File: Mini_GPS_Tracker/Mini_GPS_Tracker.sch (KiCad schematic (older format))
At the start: 19 parts, among them J1 USB_C_Receptacle, SW1 SW_Push, U1 CH340E, Y1 Crystal

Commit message: updates to routing
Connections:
- wire segments 79 -> 81
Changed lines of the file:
@@
 Wire Wire Line
 	5950 950  5950 1050
-Text GLabel 10550 4350 2    50   Input ~ 0
-GPS_TX
-Text GLabel 10550 4450 2    50   Input ~ 0
-GPS_RX
-Wire Wire Line
-	10300 4350 10550 4350
-Wire Wire Line
-	10300 4450 10550 4450
 Text GLabel 10500 5050 2    50   Input ~ 0
 TRANS_TX
@@
 Text GLabel 7650 3250 2    50   Input ~ 0
 TRANS_RX
+Wire Wire Line
+	10300 4350 10550 4350
+Wire Wire Line
+	10300 4450 10550 4450
+Text GLabel 10550 4450 2    50   Input ~ 0
+GPS_RX
+Text GLabel 10550 4350 2    50   Input ~ 0
+GPS_TX
+Text GLabel 7800 4750 2    50   Input ~ 0
+GPS_RX
+Text GLabel 7800 4650 2    50   Input ~ 0
+GPS_TX
+Wire Wire Line
+	7650 4650 7800 4650
+Wire Wire Line
+	7650 4750 7800 4750
 $EndSCHEMATC

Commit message: worked on routing
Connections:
- wire segments 81 -> 83
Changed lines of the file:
@@
 Comment4 ""
 $EndDescr
-$Sheet
-S 8950 4950 1350 500
-U 5E70A48E
-F0 "Transmitter" 50
-F1 "Transmitter.sch" 50
-F2 "TX" I R 10300 5050 50
-F3 "RX" I R 10300 5150 50
-$EndSheet
-$Sheet
-S 8950 4250 1350 500
-U 5E70A878
-F0 "GPS" 50
-F1 "GPS.sch" 50
-F2 "TX" I R 10300 4350 50
-F3 "RX" I R 10300 4450 50
-$EndSheet
-$Sheet
-S 8950 3450 1350 450
-U 5E70B79C
-F0 "Sheet5E70B79B" 50
-F1 "Power.sch" 50
-$EndSheet
 $Comp
 L Device:Crystal Y1
@@
 Wire Wire Line
 	5950 950  5950 1050
-Text GLabel 10500 5050 2    50   Input ~ 0
-TRANS_TX
-Text GLabel 10500 5150 2    50   Input ~ 0
-TRANS_RX
-Wire Wire Line
-	10300 5050 10500 5050
-Wire Wire Line
-	10300 5150 10500 5150
-Text GLabel 10400 2700 2    50   Input ~ 0
-Pressure_SCL
-Text GLabel 10400 2800 2    50   Input ~ 0
-Pressure_SDA
-Wire Wire Line
-	10350 2700 10400 2700
-Wire Wire Line
-	10350 2800 10400 2800
 $Comp
 L Sparkfun~Artemis:CH340E U1
@@
 Wire Wire Line
 	4450 4450 4450 4350
-$Sheet
-S 8900 2550 1450 550
-U 5E70BD5E
-F0 "Sheet5E70BD5D" 50
-F1 "Sensor.sch" 50
-F2 "SCL" I R 10350 2700 50
-F3 "SDA" I R 10350 2800 50
-$EndSheet
 $Comp
 L Sparkfun~Artemis:SPARKFUN_WRL-15376 MD1
@@
 Text GLabel 7650 3250 2    50   Input ~ 0
 TRANS_RX
-Wire Wire Line
-	10300 4350 10550 4350
-Wire Wire Line
-	10300 4450 10550 4450
-Text GLabel 10550 4450 2    50   Input ~ 0
-GPS_RX
-Text GLabel 10550 4350 2    50   Input ~ 0
-GPS_TX
 Text GLabel 7800 4750 2    50   Input ~ 0
 GPS_RX
@@
 Wire Wire Line
 	7650 4750 7800 4750
+Text GLabel 7850 1550 2    50   Input ~ 0
+Pressure_SDA
+Text GLabel 7850 1450 2    50   Input ~ 0
+Pressure_SCL
+Wire Wire Line
+	7650 1450 7850 1450
+Wire Wire Line
+	7650 1550 7850 1550
+Text GLabel 10650 4250 2    50   Input ~ 0
+GPS_TX
+Text GLabel 10650 4350 2    50   Input ~ 0
+GPS_RX
+Wire Wire Line
+	10400 4350 10650 4350
+Wire Wire Line
+	10400 4250 10650 4250
+$Sheet
+S 9000 2450 1450 550
+U 5E70BD5E
+F0 "Sheet5E70BD5D" 50
+F1 "Sensor.sch" 50
+F2 "SCL" I R 10450 2600 50
+F3 "SDA" I R 10450 2700 50
+$EndSheet
+Wire Wire Line
+	10450 2700 10500 2700
+Wire Wire Line
+	10450 2600 10500 2600
+Text GLabel 10500 2700 2    50   Input ~ 0
+Pressure_SDA
+Text GLabel 10500 2600 2    50   Input ~ 0
+Pressure_SCL
+Wire Wire Line
+	10400 5050 10600 5050
+Wire Wire Line
+	10400 4950 10600 4950
+Text GLabel 10600 5050 2    50   Input ~ 0
+TRANS_RX
+Text GLabel 10600 4950 2    50   Input ~ 0
+TRANS_TX
+$Sheet
+S 9050 3350 1350 450
+U 5E70B79C
+F0 "Sheet5E70B79B" 50
+F1 "Power.sch" 50
+$EndSheet
+$Sheet
+S 9050 4150 1350 500
+U 5E70A878
+F0 "GPS" 50
+F1 "GPS.sch" 50
+F2 "TX" I R 10400 4250 50
+F3 "RX" I R 10400 4350 50
+$EndSheet
+$Sheet
+S 9050 4850 1350 500
+U 5E70A48E
+F0 "Transmitter" 50
+F1 "Transmitter.sch" 50
+F2 "TX" I R 10400 4950 50
+F3 "RX" I R 10400 5050 50
+$EndSheet
 $EndSCHEMATC

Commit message: updated antenna;
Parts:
- SW1: footprint Button_Switch_SMD:SW_DIP_SPSTx01_Slide_6.7x4.1mm_W6.73mm_P2.54mm_LowProfile_JPin -> Button_Switch_SMD:SW_MEC_5GSH9
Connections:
- net labels removed: RX0
- wire segments 83 -> 85
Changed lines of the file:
@@
 $EndComp
 $Comp
-L power:GND #PWR0101
+L power:GND #PWR011
 U 1 1 5E71F955
 P 4100 2100
-F 0 "#PWR0101" H 4100 1850 50  0001 C CNN
+F 0 "#PWR011" H 4100 1850 50  0001 C CNN
 F 1 "GND" H 4105 1927 50  0000 C CNN
 F 2 "" H 4100 2100 50  0001 C CNN
@@
 $EndComp
 $Comp
-L power:GND #PWR0102
+L power:GND #PWR01
 U 1 1 5E72C86A
 P 1100 1400
-F 0 "#PWR0102" H 1100 1150 50  0001 C CNN
+F 0 "#PWR01" H 1100 1150 50  0001 C CNN
 F 1 "GND" H 1105 1227 50  0000 C CNN
 F 2 "" H 1100 1400 50  0001 C CNN
@@
 $EndComp
 $Comp
-L power:GND #PWR0103
+L power:GND #PWR05
 U 1 1 5E72D50D
 P 1800 1400
-F 0 "#PWR0103" H 1800 1150 50  0001 C CNN
+F 0 "#PWR05" H 1800 1150 50  0001 C CNN
 F 1 "GND" H 1805 1227 50  0000 C CNN
 F 2 "" H 1800 1400 50  0001 C CNN
@@
 F 0 "SW1" V 1646 2852 50  0000 R CNN
 F 1 "SW_Push" V 1555 2852 50  0000 R CNN
-F 2 "Button_Switch_SMD:SW_DIP_SPSTx01_Slide_6.7x4.1mm_W6.73mm_P2.54mm_LowProfile_JPin" H 1600 3100 50  0001 C CNN
+F 2 "Button_Switch_SMD:SW_MEC_5GSH9" H 1600 3100 50  0001 C CNN
 F 3 "~" H 1600 3100 50  0001 C CNN
 	1    1600 2900
@@
 $EndComp
 $Comp
-L power:GND #PWR0104
+L power:GND #PWR04
 U 1 1 5E737F92
 P 1600 3400
-F 0 "#PWR0104" H 1600 3150 50  0001 C CNN
+F 0 "#PWR04" H 1600 3150 50  0001 C CNN
 F 1 "GND" H 1605 3227 50  0000 C CNN
 F 2 "" H 1600 3400 50  0001 C CNN
@@
 $EndComp
 $Comp
-L power:GND #PWR0105
+L power:GND #PWR08
 U 1 1 5E738744
 P 2200 3400
-F 0 "#PWR0105" H 2200 3150 50  0001 C CNN
+F 0 "#PWR08" H 2200 3150 50  0001 C CNN
 F 1 "GND" H 2205 3227 50  0000 C CNN
 F 2 "" H 2200 3400 50  0001 C CNN
@@
 	5950 1450 6150 1450
 $Comp
-L power:+3.3V #PWR0106
+L power:+3.3V #PWR014
 U 1 1 5E73F797
 P 5950 750
-F 0 "#PWR0106" H 5950 600 50  0001 C CNN
+F 0 "#PWR014" H 5950 600 50  0001 C CNN
 F 1 "+3.3V" H 5965 923 50  0000 C CNN
 F 2 "" H 5950 750 50  0001 C CNN
@@
 $EndComp
 $Comp
-L power:GND #PWR0107
+L power:GND #PWR010
 U 1 1 5E74D69E
 P 3050 5600
-F 0 "#PWR0107" H 3050 5350 50  0001 C CNN
+F 0 "#PWR010" H 3050 5350 50  0001 C CNN
 F 1 "GND" H 3055 5427 50  0000 C CNN
 F 2 "" H 3050 5600 50  0001 C CNN
@@
 	3050 5450 3050 5600
 $Comp
-L power:+3.3V #PWR0108
+L power:+3.3V #PWR06
 U 1 1 5E74F6B2
 P 1950 4850
-F 0 "#PWR0108" H 1950 4700 50  0001 C CNN
+F 0 "#PWR06" H 1950 4700 50  0001 C CNN
 F 1 "+3.3V" H 1965 5023 50  0000 C CNN
 F 2 "" H 1950 4850 50  0001 C CNN
@@
 $EndComp
 $Comp
-L power:GND #PWR0109
+L power:GND #PWR09
 U 1 1 5E75A19B
 P 2650 6050
-F 0 "#PWR0109" H 2650 5800 50  0001 C CNN
+F 0 "#PWR09" H 2650 5800 50  0001 C CNN
 F 1 "GND" H 2655 5877 50  0000 C CNN
 F 2 "" H 2650 6050 50  0001 C CNN
@@
 	2650 6050 2650 5900
 $Comp
-L power:GND #PWR0110
+L power:GND #PWR02
 U 1 1 5E7614F5
 P 1200 7350
-F 0 "#PWR0110" H 1200 7100 50  0001 C CNN
+F 0 "#PWR02" H 1200 7100 50  0001 C CNN
 F 1 "GND" H 1205 7177 50  0000 C CNN
 F 2 "" H 1200 7350 50  0001 C CNN
@@
 $EndComp
 $Comp
-L power:GND #PWR0111
+L power:GND #PWR07
 U 1 1 5E77454B
 P 2150 6050
-F 0 "#PWR0111" H 2150 5800 50  0001 C CNN
+F 0 "#PWR07" H 2150 5800 50  0001 C CNN
 F 1 "GND" H 2155 5877 50  0000 C CNN
 F 2 "" H 2150 6050 50  0001 C CNN
@@
 	3950 5150 4150 5150
 $Comp
-L power:+3.3V #PWR0112
+L power:+3.3V #PWR012
 U 1 1 5E7841FA
 P 4200 3950
-F 0 "#PWR0112" H 4200 3800 50  0001 C CNN
+F 0 "#PWR012" H 4200 3800 50  0001 C CNN
 F 1 "+3.3V" H 4215 4123 50  0000 C CNN
 F 2 "" H 4200 3950 50  0001 C CNN
@@
 $EndComp
 $Comp
-L power:+3.3V #PWR0113
+L power:+3.3V #PWR013
 U 1 1 5E78507D
 P 4450 3950
-F 0 "#PWR0113" H 4450 3800 50  0001 C CNN
+F 0 "#PWR013" H 4450 3800 50  0001 C CNN
 F 1 "+3.3V" H 4465 4123 50  0000 C CNN
 F 2 "" H 4450 3950 50  0001 C CNN
@@
 $EndComp
 $Comp
-L power:GND #PWR0114
+L power:GND #PWR015
 U 1 1 5E7E1693
 P 7750 6400
-F 0 "#PWR0114" H 7750 6150 50  0001 C CNN
+F 0 "#PWR015" H 7750 6150 50  0001 C CNN
 F 1 "GND" H 7755 6227 50  0000 C CNN
 F 2 "" H 7750 6400 50  0001 C CNN
@@
 Wire Wire Line
 	7750 6350 7750 6400
+Text GLabel 7800 1050 2    50   Input ~ 0
+TXO
 Text GLabel 7800 1150 2    50   Input ~ 0
-TXO
-Text GLabel 7800 1050 2    50   Input ~ 0
-RX0
+RXI
+Wire Wire Line
+	7650 1150 7800 1150
 Wire Wire Line
 	7650 1050 7800 1050
-Wire Wire Line
-	7650 1150 7800 1150
-$Comp
-L power:+3.3V #PWR0115
+$Comp
+L power:+3.3V #PWR03
 U 1 1 5E7FD57A
 P 1600 1950
-F 0 "#PWR0115" H 1600 1800 50  0001 C CNN
+F 0 "#PWR03" H 1600 1800 50  0001 C CNN
 F 1 "+3.3V" H 1615 2123 50  0000 C CNN
 F 2 "" H 1600 1950 50  0001 C CNN
@@
 	1    0    0    -1
 $EndComp
-Text GLabel 7650 3150 2    50   Input ~ 0
+Text GLabel 7850 3250 2    50   Input ~ 0
 TRANS_TX
-Text GLabel 7650 3250 2    50   Input ~ 0
+Text GLabel 7850 3150 2    50   Input ~ 0
 TRANS_RX
-Text GLabel 7800 4750 2    50   Input ~ 0
+Text GLabel 7800 4650 2    50   Input ~ 0
 GPS_RX
-Text GLabel 7800 4650 2    50   Input ~ 0
-GPS_TX
-Wire Wire Line
-	7650 4650 7800 4650
 Wire Wire Line
 	7650 4750 7800 4750
@@
 F3 "RX" I R 10400 5050 50
 $EndSheet
+Wire Wire Line
+	7650 3150 7850 3150
+Wire Wire Line
+	7650 3250 7850 3250
+Wire Wire Line
+	7650 4650 7800 4650
+Text GLabel 7800 4750 2    50   Input ~ 0
+GPS_TX
 $EndSCHEMATC

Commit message: added 9dof
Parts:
- added J4: Conn_ARM_JTAG_SWD_10, Connector_PinHeader_1.00mm:PinHeader_2x05_P1.00mm_Vertical, symbol Connector:Conn_ARM_JTAG_SWD_10
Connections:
- net labels added: A1, RESET_2, SWDCK, SWDIO
- net labels removed: DTR
- wire segments 85 -> 100
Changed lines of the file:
@@
 	5900 1250 6150 1250
 Text GLabel 1000 1000 0    50   Input ~ 0
-DTR
+RTS
 Text GLabel 1900 1000 2    50   Input ~ 0
 BOOT
@@
 Connection ~ 1800 1000
 Text GLabel 850  2700 0    50   Input ~ 0
-DTR
+RTS
 Text GLabel 2300 2700 2    50   Input ~ 0
 RESET
@@
 Text GLabel 7800 4750 2    50   Input ~ 0
 GPS_TX
+$Comp
+L Connector:Conn_ARM_JTAG_SWD_10 J4
+U 1 1 5E76D592
+P 4950 6900
+F 0 "J4" H 4507 6946 50  0000 R CNN
+F 1 "Conn_ARM_JTAG_SWD_10" H 4507 6855 50  0000 R CNN
+F 2 "Connector_PinHeader_1.00mm:PinHeader_2x05_P1.00mm_Vertical" H 4950 6900 50  0001 C CNN
+F 3 "http://infocenter.arm.com/help/topic/com.arm.doc.ddi0314h/DDI0314H_coresight_components_trm.pdf" V 4600 5650 50  0001 C CNN
+	1    4950 6900
+	1    0    0    -1
+$EndComp
+$Comp
+L power:+3.3V #PWR030
+U 1 1 5E76F259
+P 4950 6150
+F 0 "#PWR030" H 4950 6000 50  0001 C CNN
+F 1 "+3.3V" H 4965 6323 50  0000 C CNN
+F 2 "" H 4950 6150 50  0001 C CNN
+F 3 "" H 4950 6150 50  0001 C CNN
+	1    4950 6150
+	1    0    0    -1
+$EndComp
+$Comp
+L power:GND #PWR031
+U 1 1 5E76F975
+P 4950 7600
+F 0 "#PWR031" H 4950 7350 50  0001 C CNN
+F 1 "GND" H 4955 7427 50  0000 C CNN
+F 2 "" H 4950 7600 50  0001 C CNN
+F 3 "" H 4950 7600 50  0001 C CNN
+	1    4950 7600
+	1    0    0    -1
+$EndComp
+Wire Wire Line
+	4950 7500 4950 7550
+Wire Wire Line
+	4850 7500 4850 7550
+Wire Wire Line
+	4850 7550 4950 7550
+Connection ~ 4950 7550
+Wire Wire Line
+	4950 7550 4950 7600
+Wire Wire Line
+	4950 6300 4950 6150
+Text GLabel 5600 7000 2    50   Input ~ 0
+A1
+Text GLabel 5550 6600 2    50   Input ~ 0
+RESET_2
+Text GLabel 5600 6900 2    50   Input ~ 0
+SWDIO
+Text GLabel 5600 6800 2    50   Input ~ 0
+SWDCK
+Wire Wire Line
+	5450 6600 5550 6600
+Wire Wire Line
+	5450 6800 5600 6800
+Wire Wire Line
+	5450 6900 5600 6900
+Wire Wire Line
+	5450 7000 5600 7000
+Wire Wire Line
+	4950 7550 5550 7550
+Wire Wire Line
+	5550 7550 5550 7100
+Wire Wire Line
+	5550 7100 5450 7100
+Text GLabel 7850 2950 2    50   Input ~ 0
+SWDIO
+Text GLabel 7850 3050 2    50   Input ~ 0
+SWDCK
+Wire Wire Line
+	7650 2950 7850 2950
+Wire Wire Line
+	7650 3050 7850 3050
+Text GLabel 7800 3850 2    50   Input ~ 0
+A1
+Wire Wire Line
+	7650 3850 7800 3850
 $EndSCHEMATC

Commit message: schamatics finalized
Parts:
- removed C2: CAP, Capacitor_SMD:C_0805_2012Metric_Pad1.15x1.40mm_HandSolder, symbol pspice:CAP
- removed R1: DNP, symbol Device:R
- removed R3: 220K, Resistor_SMD:R_0805_2012Metric_Pad1.15x1.40mm_HandSolder, symbol Device:R
- added H1, H2, H3, H4: MountingHole_Pad, MountingHole:MountingHole_3.2mm_M3, symbol Mechanical:MountingHole_Pad
- SW1: footprint Button_Switch_SMD:SW_MEC_5GSH9 -> Sparkfun-Artemis:SW_TL1015AF160QG
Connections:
- net labels added: 9_SCL, 9_SDA, MISO_Flash, MOSI_Flash, clk_flash, cs_flash, gps_reset, v_measure
- net labels removed: BOOT, RESET_2, TXO, nReset
- wire segments 100 -> 113
- no-connect marks 0 -> 47
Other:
- moved on the sheet: J4

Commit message: added routing
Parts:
- added LS1: CSS-J4D20-SMT, Sparkfun-Artemis:CUI_CSS-J4D20-SMT, symbol Sparkfun~Artemis:CSS-J4D20-SMT
- added R7: R, Resistor_SMD:R_0805_2012Metric_Pad1.15x1.40mm_HandSolder, symbol Device:R
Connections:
- net labels added: buzzer
- wire segments 113 -> 117
- no-connect marks 47 -> 46
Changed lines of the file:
@@
 NoConn ~ 7650 3550
 NoConn ~ 7650 3450
-NoConn ~ 7650 3350
 NoConn ~ 7650 2850
 NoConn ~ 7650 2750
@@
 Wire Wire Line
 	7650 1750 7850 1750
+$Comp
+L Sparkfun~Artemis:CSS-J4D20-SMT LS1
+U 1 1 5E7E01A2
+P 5300 3750
+F 0 "LS1" H 5405 3796 50  0000 L CNN
+F 1 "CSS-J4D20-SMT" H 5405 3705 50  0000 L CNN
+F 2 "Sparkfun-Artemis:CUI_CSS-J4D20-SMT" H 5300 3750 50  0001 L BNN
+F 3 "CUI" H 5300 3750 50  0001 L BNN
+F 4 "None" H 5300 3750 50  0001 L BNN "Field4"
+F 5 "CSS-J4D20-SMT" H 5300 3750 50  0001 L BNN "Field5"
+F 6 "Unavailable" H 5300 3750 50  0001 L BNN "Field6"
+F 7 "8.5 mm, 3.6 V, 90 dB, Surface Mount _SMT_, Magnetic Audio Transducer Buzzer" H 5300 3750 50  0001 L BNN "Field7"
+F 8 "None" H 5300 3750 50  0001 L BNN "Field8"
+	1    5300 3750
+	1    0    0    -1
+$EndComp
+$Comp
+L Device:R R7
+U 1 1 5E7E2738
+P 5300 3300
+F 0 "R7" H 5370 3346 50  0000 L CNN
+F 1 "R" H 5370 3255 50  0000 L CNN
+F 2 "Resistor_SMD:R_0805_2012Metric_Pad1.15x1.40mm_HandSolder" V 5230 3300 50  0001 C CNN
+F 3 "~" H 5300 3300 50  0001 C CNN
+	1    5300 3300
+	1    0    0    -1
+$EndComp
+$Comp
+L power:GND #PWR0116
+U 1 1 5E7E36E3
+P 5300 4050
+F 0 "#PWR0116" H 5300 3800 50  0001 C CNN
+F 1 "GND" H 5305 3877 50  0000 C CNN
+F 2 "" H 5300 4050 50  0001 C CNN
+F 3 "" H 5300 4050 50  0001 C CNN
+	1    5300 4050
+	1    0    0    -1
+$EndComp
+Wire Wire Line
+	5300 3950 5300 4050
+Wire Wire Line
+	5300 3550 5300 3450
+Text GLabel 5300 3000 1    50   Input ~ 0
+buzzer
+Wire Wire Line
+	5300 3000 5300 3150
+Text GLabel 7850 3350 2    50   Input ~ 0
+buzzer
+Wire Wire Line
+	7650 3350 7850 3350
 $EndSCHEMATC

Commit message: all  artemis connections routed
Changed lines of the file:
@@
 Wire Wire Line
 	7750 6350 7750 6400
-Text GLabel 7800 1050 2    50   Input ~ 0
-TX0
-Text GLabel 7800 1150 2    50   Input ~ 0
-RXI
-Wire Wire Line
-	7650 1150 7800 1150
-Wire Wire Line
-	7650 1050 7800 1050
 $Comp
 L power:+3.3V #PWR03
@@
 	1    0    0    -1
 $EndComp
-Text GLabel 7850 3250 2    50   Input ~ 0
-TRANS_TX
+Text GLabel 7800 3550 2    50   Input ~ 0
+TRANS_RX
 Text GLabel 7850 3150 2    50   Input ~ 0
-TRANS_RX
-Text GLabel 7800 4650 2    50   Input ~ 0
 GPS_RX
-Wire Wire Line
-	7650 4750 7800 4750
-Text GLabel 7850 1550 2    50   Input ~ 0
+Text GLabel 7800 3450 2    50   Input ~ 0
 Pressure_SDA
-Text GLabel 7850 1450 2    50   Input ~ 0
-Pressure_SCL
 Wire Wire Line
 	7650 1450 7850 1450
@@
 Wire Wire Line
 	7650 4650 7800 4650
-Text GLabel 7800 4750 2    50   Input ~ 0
+Text GLabel 7850 3250 2    50   Input ~ 0
 GPS_TX
 $Comp
@@
 Wire Wire Line
 	7650 2550 7800 2550
-Text GLabel 7800 5050 2    50   Input ~ 0
+Text GLabel 7850 1450 2    50   Input ~ 0
 9_SCL
-Text GLabel 7800 5150 2    50   Input ~ 0
+Text GLabel 7850 1550 2    50   Input ~ 0
 9_SDA
-Wire Wire Line
-	7650 5050 7800 5050
-Wire Wire Line
-	7650 5150 7800 5150
-Text GLabel 7800 5250 2    50   Input ~ 0
+Text GLabel 7800 2450 2    50   Input ~ 0
 gps_reset
-Wire Wire Line
-	7650 5250 7800 5250
-NoConn ~ 7650 5550
 NoConn ~ 7650 5450
 NoConn ~ 7650 4950
 NoConn ~ 7650 4850
 NoConn ~ 7650 4550
-NoConn ~ 7650 4450
 NoConn ~ 7650 4350
 NoConn ~ 7650 4250
@@
 NoConn ~ 7650 3950
 NoConn ~ 7650 3750
-NoConn ~ 7650 3650
-NoConn ~ 7650 3550
-NoConn ~ 7650 3450
 NoConn ~ 7650 2850
 NoConn ~ 7650 2750
 NoConn ~ 7650 2650
-NoConn ~ 7650 2450
 NoConn ~ 7650 2350
-NoConn ~ 7650 2250
 NoConn ~ 7650 2150
 NoConn ~ 7650 2050
 NoConn ~ 7650 1350
 NoConn ~ 7650 1250
-NoConn ~ 7650 950
 Text GLabel 5900 1250 0    50   Input ~ 0
 RESET
@@
 Wire Wire Line
 	10450 5900 10600 5900
-Text GLabel 7800 1950 2    50   Input ~ 0
+Text GLabel 7800 4650 2    50   Input ~ 0
 MOSI_Flash
-Text GLabel 7800 1850 2    50   Input ~ 0
+Text GLabel 7800 5150 2    50   Input ~ 0
 MISO_Flash
-Wire Wire Line
-	7650 1850 7800 1850
-Wire Wire Line
-	7650 1950 7800 1950
-Text GLabel 7850 1750 2    50   Input ~ 0
+Text GLabel 7800 950  2    50   Input ~ 0
 cs_flash
-Text GLabel 7850 1650 2    50   Input ~ 0
+Text GLabel 7800 5050 2    50   Input ~ 0
 clk_flash
-Wire Wire Line
-	7650 1650 7850 1650
-Wire Wire Line
-	7650 1750 7850 1750
 $Comp
 L Sparkfun~Artemis:CSS-J4D20-SMT LS1
@@
 Wire Wire Line
 	5300 3000 5300 3150
-Text GLabel 7850 3350 2    50   Input ~ 0
+Text GLabel 7800 5550 2    50   Input ~ 0
 buzzer
 Wire Wire Line
-	7650 3350 7850 3350
+	7650 1050 7800 1050
+Wire Wire Line
+	7650 1150 7800 1150
+Text GLabel 7800 1150 2    50   Input ~ 0
+RXI
+Text GLabel 7800 1050 2    50   Input ~ 0
+TX0
+NoConn ~ 7650 3350
+Wire Wire Line
+	7650 5550 7800 5550
+NoConn ~ 7650 5250
+Text GLabel 7800 3650 2    50   Input ~ 0
+Pressure_SCL
+Text GLabel 7750 2250 2    50   Input ~ 0
+TRANS_TX
+Wire Wire Line
+	7750 2250 7650 2250
+Wire Wire Line
+	7800 2450 7650 2450
+Wire Wire Line
+	7800 3450 7650 3450
+Wire Wire Line
+	7650 3550 7800 3550
+Wire Wire Line
+	7800 3650 7650 3650
+Wire Wire Line
+	7650 5050 7800 5050
+Wire Wire Line
+	7650 5150 7800 5150
+NoConn ~ 7650 4750
+NoConn ~ 7650 1650
+NoConn ~ 7650 1750
+NoConn ~ 7650 1850
+NoConn ~ 7650 1950
+NoConn ~ 7650 4450
+Wire Wire Line
+	7650 950  7800 950
 $EndSCHEMATC

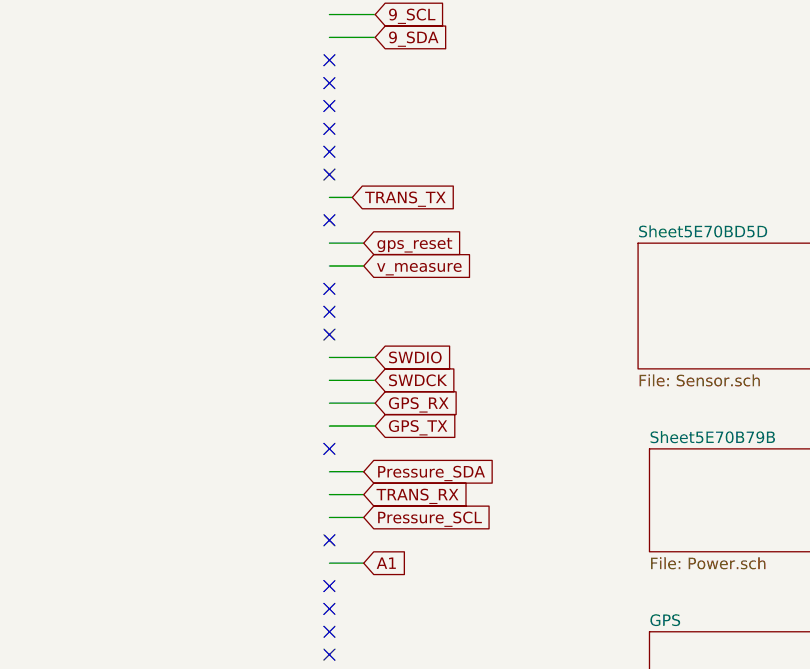
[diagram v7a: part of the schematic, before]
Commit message: fixed tx route
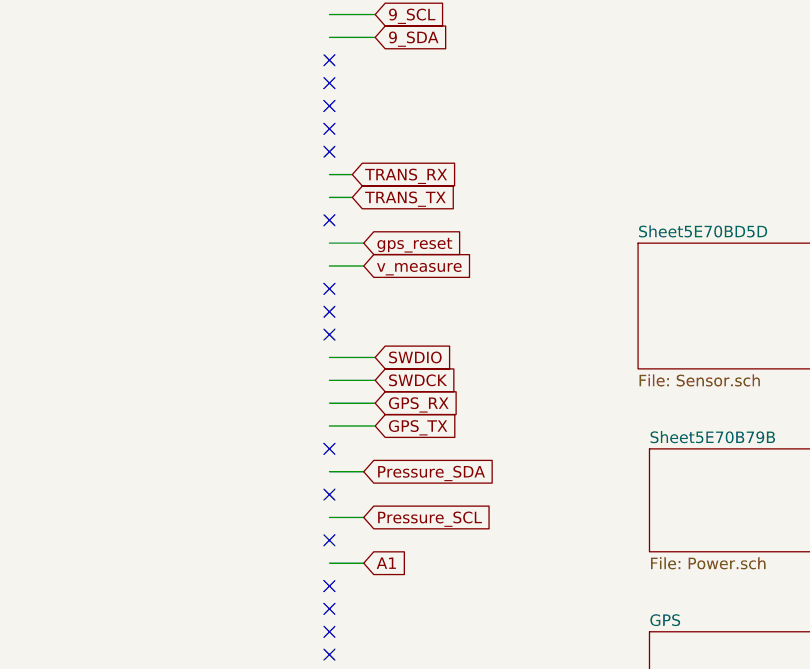
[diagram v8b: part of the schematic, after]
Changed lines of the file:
@@
 	1    0    0    -1
 $EndComp
-Text GLabel 7800 3550 2    50   Input ~ 0
+Text GLabel 7750 2150 2    50   Input ~ 0
 TRANS_RX
 Text GLabel 7850 3150 2    50   Input ~ 0
@@
 NoConn ~ 7650 2650
 NoConn ~ 7650 2350
-NoConn ~ 7650 2150
 NoConn ~ 7650 2050
 NoConn ~ 7650 1350
@@
 	7800 3450 7650 3450
 Wire Wire Line
-	7650 3550 7800 3550
-Wire Wire Line
 	7800 3650 7650 3650
 Wire Wire Line
@@
 Wire Wire Line
 	7650 950  7800 950
+NoConn ~ 7650 3550
+Wire Wire Line
+	7650 2150 7750 2150
 $EndSCHEMATC
